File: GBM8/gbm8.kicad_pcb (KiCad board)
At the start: 2 copper layers, 47.4 x 99.7 mm, 72 parts, among them K101 CONN_31-SPEC, K201 RJ45-MAGJACK, K401 ISP6, Q201 BC848, U1 ATXMEGAXA4U, U2 ENC424J600, U401 LD1117, X401 25MHz, X402 32MHz

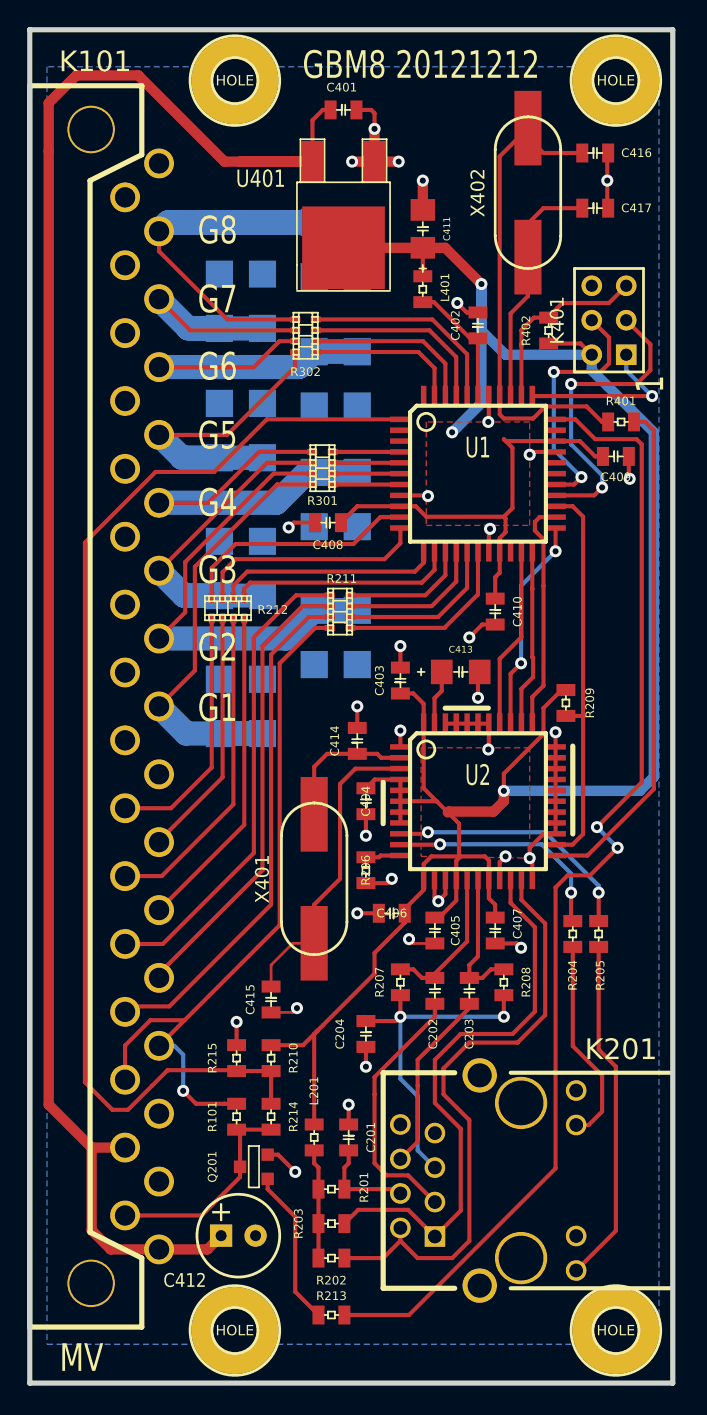
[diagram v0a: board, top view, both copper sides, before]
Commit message: GBM8 Rev. B 2022-01-12 Remove ENC424J600 Add Isolated supply and communication interface
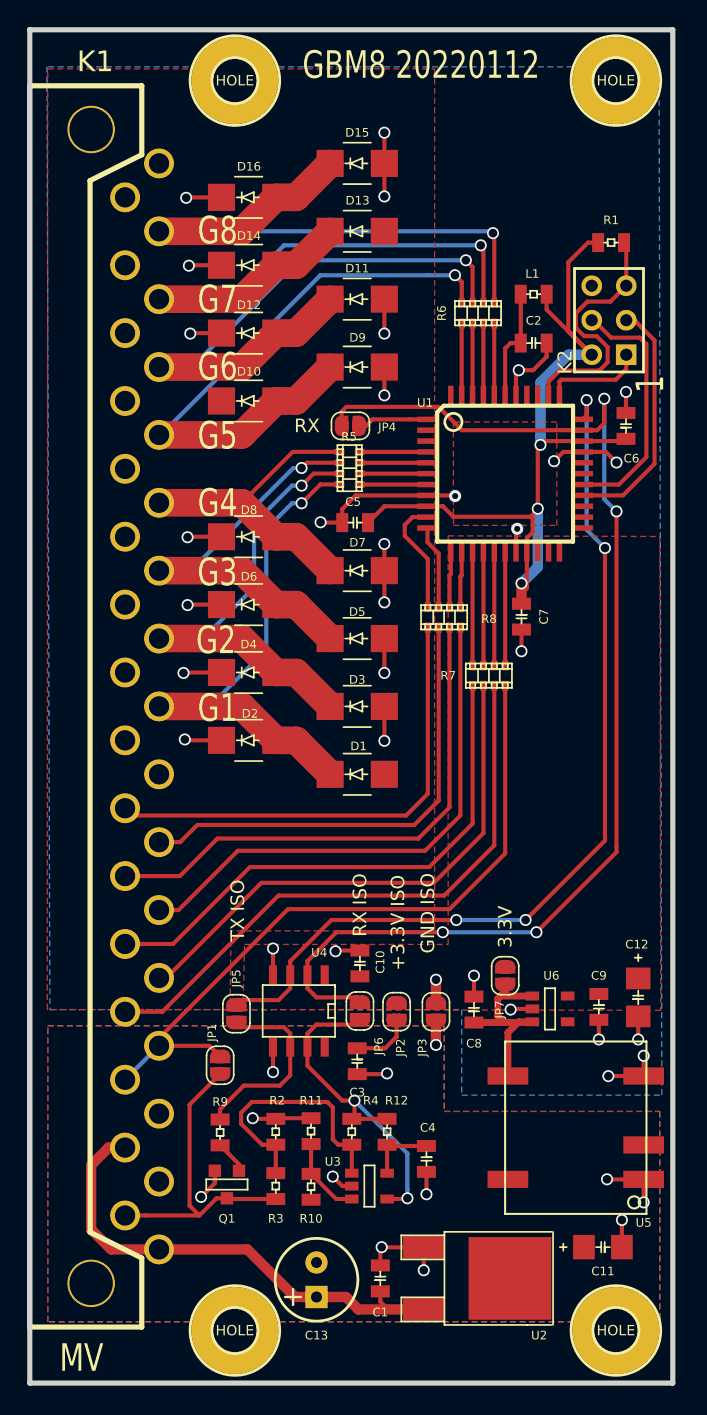
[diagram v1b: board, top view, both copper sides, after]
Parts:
- removed C201, C204, C401, C402, C403, C404, C405, C406, C407, C409, C410: 100nF, base:C0805
- removed C202, C203: 6.8nF, base:C0805
- removed C411, C413: 10uF, base:C1206Pol
- removed C414, C415, C416, C417: 27pF, base:C0805
- removed D302: DIODE, base:DSMA
- removed K101: CONN_31-SPEC, base:DIN41617-31-spec
- removed K201: RJ45-MAGJACK, base:RJ45_Magjack
- removed K401: ISP6, base:header_3x2
- removed L201: EMI Filter Bead, base:R0805
- removed Q201: BC848, base:SOT23EBC
- removed R101, R401: 0R, base:R0805
- removed R201: 10R, base:R0805
- removed R202, R203, R207, R208: 50R, base:R0805
- removed R204, R205: 330R, base:R0805
- removed R206: 12k4, base:R0805
- removed R209: 100k, base:R0805
- removed R210, R215: 10k, base:R0805
- removed R211, R212: 1k, base:R1206x4
- removed R213: 1k, base:R0805
- removed R214: 68k, base:R0805
- removed U401: LD1117, base:DPAK2-Reg
- removed X401: 25MHz, base:HC49S_SMD
- removed X402: 32MHz, base:HC49S_SMD
- added C1: 100nF, base:C0805, F.Cu at (156.0, 143.1)
- added C10: 100nF, base:C0805, F.Cu at (154.5, 119.9)
- added C11: 10uF, base:C1206Pol, F.Cu at (172.4, 140.8)
- added C12: 10uF, base:C1206Pol, F.Cu at (175.0, 122.4)
- added C2: 100nF, base:C0805, F.Cu at (167.3, 74.2)
- added C3: 100nF, base:C0805, F.Cu at (154.3, 127.1)
- added C4: 100nF, base:C0805, F.Cu at (159.4, 134.3)
- added C6: 100nF, base:C0805, F.Cu at (174.1, 80.3)
- added C7: 100nF, base:C0805, F.Cu at (166.4, 94.4)
- added C8: 100nF, base:C0805, F.Cu at (162.9, 123.3)
- added C9: 100nF, base:C0805, F.Cu at (172.1, 123.1)
- added D2: DIODE, base:DSMA, F.Cu at (146.3, 103.5)
- added JP1: Option 1, base:SolderJumper-2_P1.3mm_Open_RoundedPad1.0x1.5mm, F.Cu at (144.2, 127.4)
- added JP2: +3.3V ISO, base:SolderJumper-2_P1.3mm_Open_RoundedPad1.0x1.5mm, F.Cu at (157.2, 123.5)
- added JP3: GND ISO, base:SolderJumper-2_P1.3mm_Open_RoundedPad1.0x1.5mm, F.Cu at (160.1, 123.5)
- added JP4: RX, base:SolderJumper-2_P1.3mm_Open_RoundedPad1.0x1.5mm, F.Cu at (153.8, 80.3)
- added JP5: TX ISO, base:SolderJumper-2_P1.3mm_Open_RoundedPad1.0x1.5mm, F.Cu at (145.4, 123.6)
- added JP6: RX ISO, base:SolderJumper-2_P1.3mm_Open_RoundedPad1.0x1.5mm, F.Cu at (154.5, 123.4)
- added JP7: 3.3V, base:SolderJumper-2_P1.3mm_Open_RoundedPad1.0x1.5mm, F.Cu at (165.2, 120.8)
- added K1: DIN41617, base:DIN41617-31-spec, F.Cu at (139.7, 101.0)
- added K2: ISP6, base:header_3x2, F.Cu at (172.8, 72.5)
- added Q1: BC848, base:SOT23EBC, F.Cu at (144.7, 136.2)
- added R10: 10k, base:R0805, F.Cu at (150.9, 136.4)
- added R11: 10k, base:R0805, F.Cu at (150.9, 132.3)
- added R12: 10k, base:R0805, F.Cu at (156.5, 132.3)
- added R2: 150k, base:R0805, F.Cu at (148.3, 132.3)
- added R3: 240k, base:R0805, F.Cu at (148.3, 136.3)
- added R4: 240k, base:R0805, F.Cu at (153.9, 132.3)
- added R7: 1k, base:R1206x4, F.Cu at (164.0, 98.7)
- added R8: 1k, base:R1206x4, F.Cu at (160.7, 94.4)
- added R9: 1k, base:R0805, F.Cu at (144.2, 132.3)
- added U3: LMV331, base:SOT23-5, F.Cu at (155.2, 136.3)
- added U4: ADuM7241, base:SO8E, F.Cu at (150.0, 123.4)
- added U5: NXE1, base:NXE1, F.Cu at (170.4, 132.0)
- added U6: LP2985, base:SOT23-5, F.Cu at (168.5, 123.2)
- D1: renamed from D301; moved to F.Cu
- D10: renamed from D310; moved to F.Cu
- D11: renamed from D311; moved to F.Cu
- D12: renamed from D312; moved to F.Cu
- D13: renamed from D313; moved to F.Cu
- D14: renamed from D314; moved to F.Cu
- D15: renamed from D315; moved to F.Cu
- D16: renamed from D316; moved to F.Cu
- D3: renamed from D303; moved to F.Cu
- D4: renamed from D304; moved to F.Cu
- D5: renamed from D305; moved to F.Cu
- D6: renamed from D306; moved to F.Cu
- D7: renamed from D307; moved to F.Cu
- D8: renamed from D308; moved to F.Cu
- D9: renamed from D309; moved to F.Cu
- U2: value ENC424J600 -> LD1117; footprint base:TQFP44 -> base:DPAK2-Reg
- moved U2 35.4 mm to (159.2, 143.1), turned to 270 degrees
- moved R6 12.8 mm to (163.2, 72.0), turned to 90 degrees
- moved D5 11.4 mm to (154.3, 96.0), turned to 0 degrees
- moved D13 11.4 mm to (154.3, 66.0), turned to 0 degrees
- moved D1 11.3 mm to (154.3, 106.0), turned to 0 degrees
- moved D9 11.2 mm to (154.3, 76.0), turned to 0 degrees
- moved D16 8.88 mm to (146.3, 63.5), turned to 0 degrees
- moved D12 8.68 mm to (146.3, 73.5), turned to 0 degrees
- moved D8 8.46 mm to (146.3, 88.5), turned to 0 degrees
- moved D4 8.41 mm to (146.3, 98.5), turned to 0 degrees
- moved L1 8.18 mm to (167.3, 70.6), turned to 180 degrees
- moved R1 7.94 mm to (173.0, 66.8), turned to 0 degrees
- moved D15 7.09 mm to (154.3, 61.0), turned to 0 degrees
- moved D11 6.67 mm to (154.3, 71.0), turned to 0 degrees
- moved C13 6.61 mm to (151.3, 143.2), turned to 90 degrees
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- renumbered C412 to C13, C408 to C5, L401 to L1, R402 to R1, R301 to R5, R302 to R6
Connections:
- C13 pad 1: Vin -> /Vin
- C13 pad 2: GND -> GND_ISO
- U1 pad 1: CommRX -> /CommRX
- U1 pad 2: Net-(U1-Pad2) -> (no net)
- U1 pad 20: Net-(U1-Pad20) -> (no net)
- U1 pad 21: /Interface/SCK -> (no net)
- U1 pad 22: /Interface/MISO -> (no net)
- U1 pad 23: /Interface/MOSI -> (no net)
- U1 pad 24: /Interface/CS -> (no net)
- U1 pad 25: /Interface/INT -> (no net)
- U1 pad 28: Net-(U1-Pad28) -> (no net)
- U1 pad 29: Net-(U1-Pad29) -> (no net)
- U1 pad 3: Net-(U1-Pad3) -> (no net)
- U1 pad 32: Net-(U1-Pad32) -> /LN_RX
- U1 pad 33: CommTX -> /LN_TX
- U1 pad 36: Net-(C417-Pad1) -> (no net)
- U1 pad 37: Net-(C416-Pad1) -> (no net)
- U1 pad 44: Net-(U1-Pad44) -> (no net)
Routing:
- net +3.3V: track 198.2 -> 64.9 mm
- net Vin: track 130.3 -> 0.00 mm
- net /LN_RX: track 0.00 -> 89.4 mm, vias 0 -> 4
- net CommTX: track 85.3 -> 0.00 mm, vias 2 -> 0
- net CommRX: track 85.0 -> 0.00 mm
- net /LN_TX: track 0.00 -> 67.9 mm, vias 0 -> 4
- net Net-(K201-Pad2): track 45.1 -> 0.00 mm
- net Net-(K201-Pad1): track 41.9 -> 0.00 mm
- net /Vin: track 0.00 -> 38.9 mm
- net Net-(R401-Pad2): track 37.4 -> 0.00 mm
- net Net-(C416-Pad1): track 36.1 -> 0.00 mm
- net /Interface/INT: track 29.3 -> 0.00 mm
- net GND_ISO: track 0.00 -> 28.5 mm, vias 0 -> 12
- net Net-(C204-Pad1): track 25.6 -> 0.00 mm, vias 2 -> 0
- net Net-(K201-PadGA): track 25.6 -> 0.00 mm
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- added copper zone on F.Cu, net +3.3V_ISO
- added copper zone on F.Cu, net GND
- added copper zone on B.Cu, net GND_ISO
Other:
- board text added: "GBM8 20220112"
- board text removed: "GBM8 20121212"
